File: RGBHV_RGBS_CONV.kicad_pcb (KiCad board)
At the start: 2 copper layers, 100 x 100 mm, 42 parts, among them J1 DIGITAL RGB, J10 ENABLE_SYNC_DIVIDE, J11 RGBHV_2, J12 LOGIC_SINGLE, J13 LOGIC_DOUBLE, J14 ENABLE_SYNC_MARGE, J15 RGBS_2, J16 RGBS_1, J17 +5V IN, J18 +5V OUT, J2 VGA DB15, J3 ANALOG RGB DB15, J4 X1, J5 DIGITAL_RGBHV_1, J6 ANALOG RGB, J7 DIGITAL_RGBHV_2, J8 ANALOG RGB VGA, J9 RGBHV_1, U1 LM1881, U2 74HC86

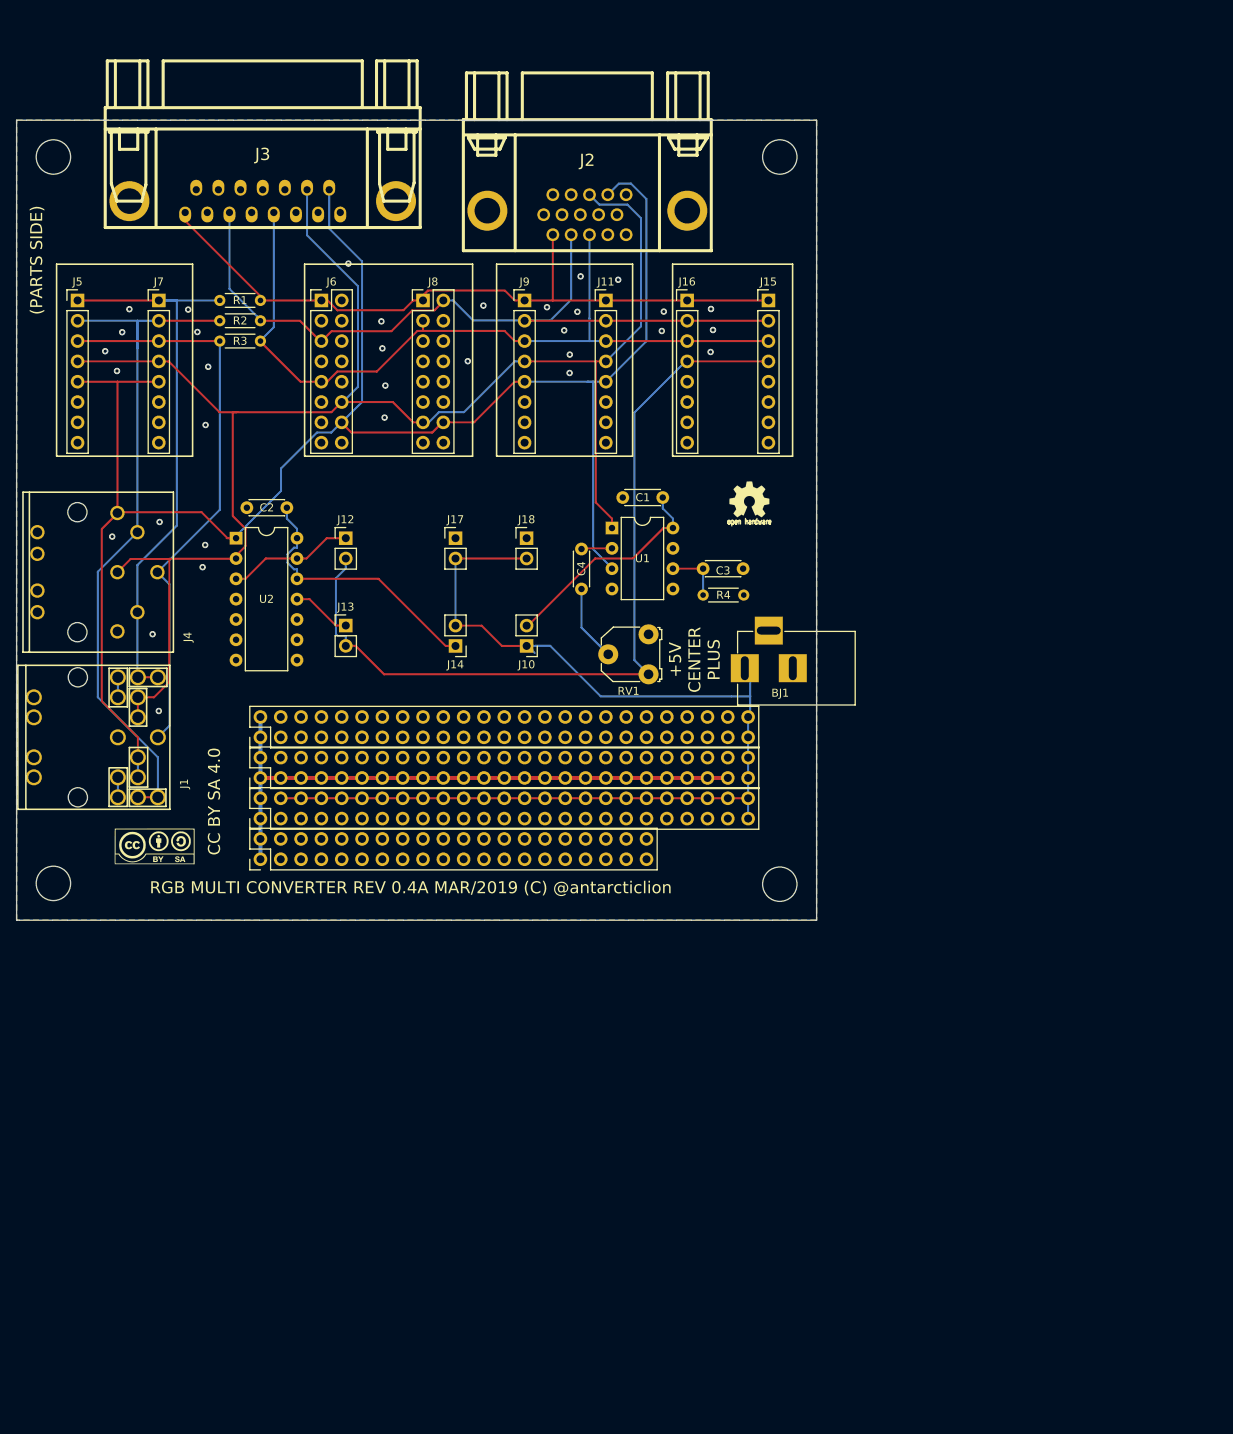
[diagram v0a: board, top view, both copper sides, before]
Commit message: Rev.5A DIn8 fix and remove sync sep.
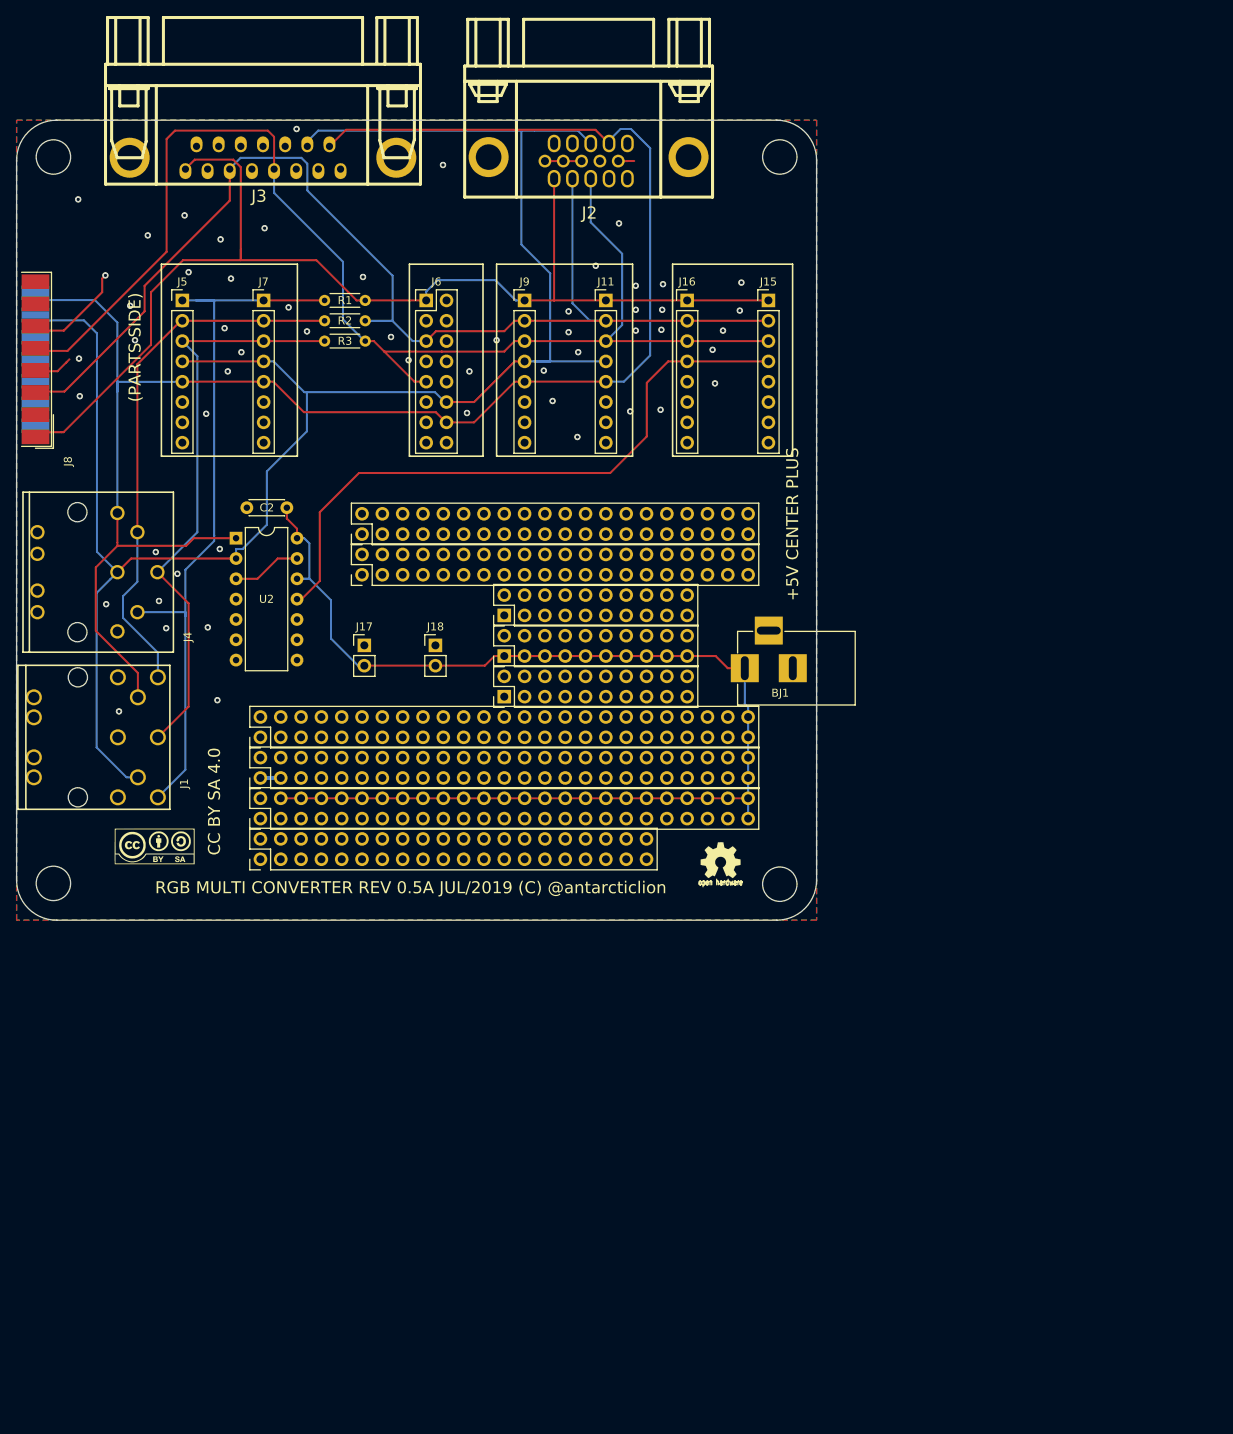
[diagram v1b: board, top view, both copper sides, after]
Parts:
- removed C1, C3, C4: 0.1uF, Capacitors_ThroughHole:C_Disc_D4.3mm_W1.9mm_P5.00mm
- removed J10: ENABLE_SYNC_DIVIDE, Pin_Headers:Pin_Header_Straight_1x02_Pitch2.54mm
- removed J12: LOGIC_SINGLE, Pin_Headers:Pin_Header_Straight_1x02_Pitch2.54mm
- removed J13: LOGIC_DOUBLE, Pin_Headers:Pin_Header_Straight_1x02_Pitch2.54mm
- removed J14: ENABLE_SYNC_MARGE, Pin_Headers:Pin_Header_Straight_1x02_Pitch2.54mm
- removed R4: 680KR, Resistors_ThroughHole:R_Axial_DIN0204_L3.6mm_D1.6mm_P5.08mm_Horizontal
- removed RV1: 1KR, Potentiometers:Potentiometer_Triwood_RM-065
- removed U1: LM1881, Housings_DIP:DIP-8_W7.62mm
- added JA5: PinHeader_2x10_P2.54mm_Vertical, Connector_PinHeader_2.54mm:PinHeader_2x10_P2.54mm_Vertical, F.Cu at (61.0, 72.1)
- added JA6: PinHeader_2x10_P2.54mm_Vertical, Connector_PinHeader_2.54mm:PinHeader_2x10_P2.54mm_Vertical, F.Cu at (61.0, 67.0)
- added JA7: PinHeader_2x10_P2.54mm_Vertical, Connector_PinHeader_2.54mm:PinHeader_2x10_P2.54mm_Vertical, F.Cu at (61.0, 61.9)
- added JA8: Pin_Header_Straight_2x20_Pitch2.54mm, Pin_Headers:Pin_Header_Straight_2x20_Pitch2.54mm, F.Cu at (43.2, 56.8)
- added JA9: Pin_Header_Straight_2x20_Pitch2.54mm, Pin_Headers:Pin_Header_Straight_2x20_Pitch2.54mm, F.Cu at (43.2, 51.7)
- C2: value 0.1uF -> C
- J15: value RGBS_2 -> RGBS_OUT
- J16: value RGBS_1 -> RGBS_OUT
- J3: value ANALOG RGB DB15 -> ANALOG RGB DA15
- J8: value ANALOG RGB VGA -> ANALOG RGB DA15 EDGE; footprint Pin_Headers:Pin_Header_Straight_2x08_Pitch2.54mm -> Connector_Dsub:DSUB-15_Female_EdgeMount_P2.77mm
- moved J8 49.0 mm to (2.36, 29.9), turned to 270 degrees
- moved G3 45.2 mm to (88.0, 92.5)
- moved G4 45.0 mm to (89.0, 92.5)
- moved J17 17.6 mm to (43.5, 65.6)
- moved J18 17.6 mm to (52.4, 65.6)
- moved J6 13.1 mm to (51.2, 22.5)
- moved R1 13.1 mm to (38.5, 22.5)
- moved R2 13.1 mm to (38.5, 25.1)
- moved R3 13.1 mm to (38.5, 27.6)
- moved J5 13.1 mm to (20.7, 22.5)
- moved J7 13.1 mm to (30.9, 22.5)
- moved J2 6.70 mm to (71.5, -5.50)
- moved J3 5.42 mm to (30.8, -2.42)
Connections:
- C2 pad 1: Net-(C2-Pad1) -> +5V
- J2 pad : GND -> (no net)
- J3 pad : GND -> (no net)
- J8 pad 10: GND -> Net-(J8-Pad10)
- J8 pad 11: GND -> Net-(J8-Pad11)
- J8 pad 13: HSYNC -> Net-(J8-Pad13)
- J8 pad 14: VSYNC -> HSYNC
- J8 pad 15: Net-(J8-Pad15) -> VSYNC
- J8 pad 2: G -> GND
- J8 pad 3: B -> G
- J8 pad 4: Net-(J8-Pad4) -> GND
- J8 pad 5: Net-(J8-Pad5) -> B
- J8 pad 7: GND -> Net-(J8-Pad7)
- J8 pad 8: GND -> Net-(J8-Pad8)
- U2 pad 11: Net-(J13-Pad1) -> CSYNC
- U2 pad 12: Net-(C2-Pad1) -> +5V
- U2 pad 14: Net-(C2-Pad1) -> +5V
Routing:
- net B: track 100.1 -> 160.5 mm
- net R: track 89.5 -> 144.7 mm
- net G: track 98.0 -> 150.7 mm
- net GND: track 76.4 -> 25.3 mm, vias 33 -> 56
- net Net-(C2-Pad1): track 34.1 -> 0.00 mm
- net Net-(C1-Pad1): track 27.7 -> 0.00 mm
- net HSYNC: track 210.7 -> 235.5 mm
- net CSYNC: track 104.7 -> 80.2 mm
- net DIGITAL_G: track 88.5 -> 67.3 mm
- net DIGITAL_R: track 72.4 -> 91.5 mm
- net +5V: track 136.3 -> 153.9 mm
- net Net-(C4-Pad1): track 9.55 -> 0.00 mm
- net Net-(J13-Pad1): track 7.46 -> 0.00 mm
- net Net-(U2-Pad13): track 15.8 -> 8.67 mm
- net Net-(C3-Pad1): track 7.07 -> 0.00 mm
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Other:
- outline, holes or cut-outs redrawn
- board text added: "RGB MULTI CONVERTER REV 0.5A JUL/2019 (C) @antarcticlion"
- board text removed: "RGB MULTI CONVERTER REV 0.4A MAR/2019 (C) @antarcticlion"

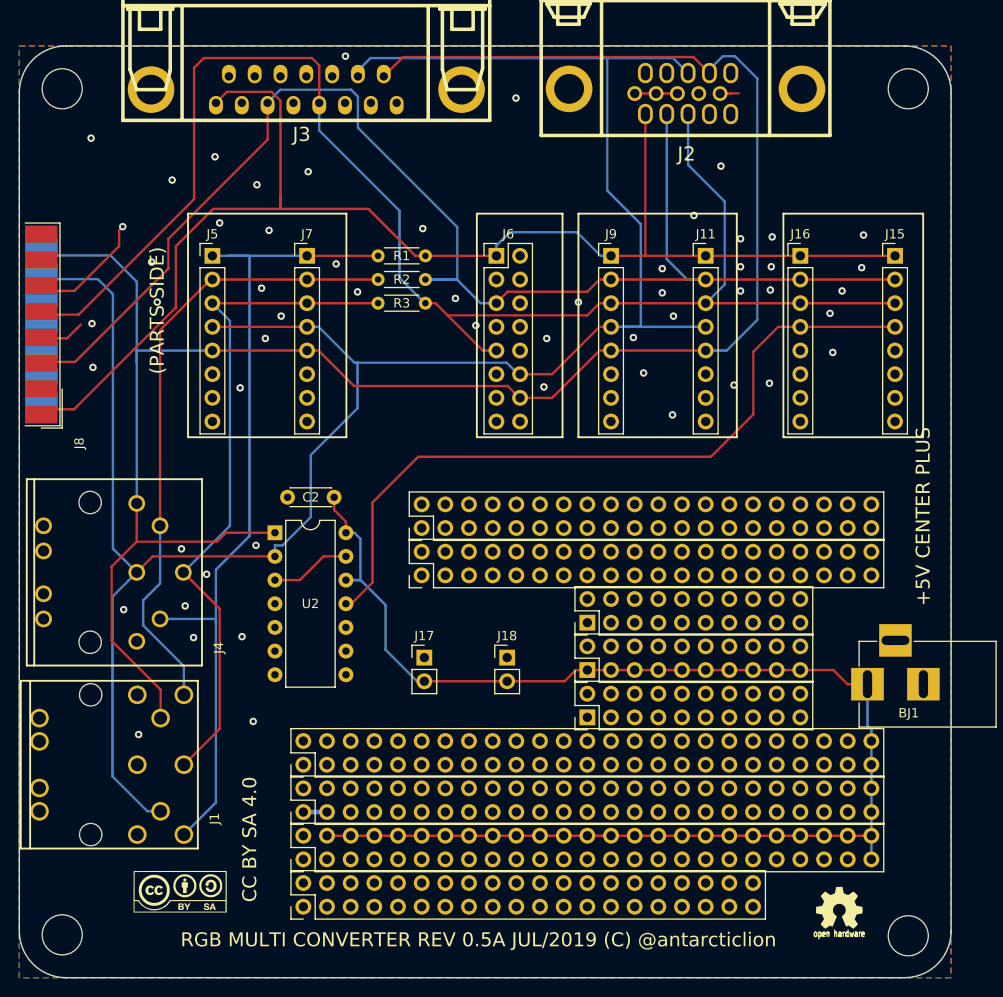
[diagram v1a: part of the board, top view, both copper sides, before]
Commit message: Rev.5B Add RGBS VR
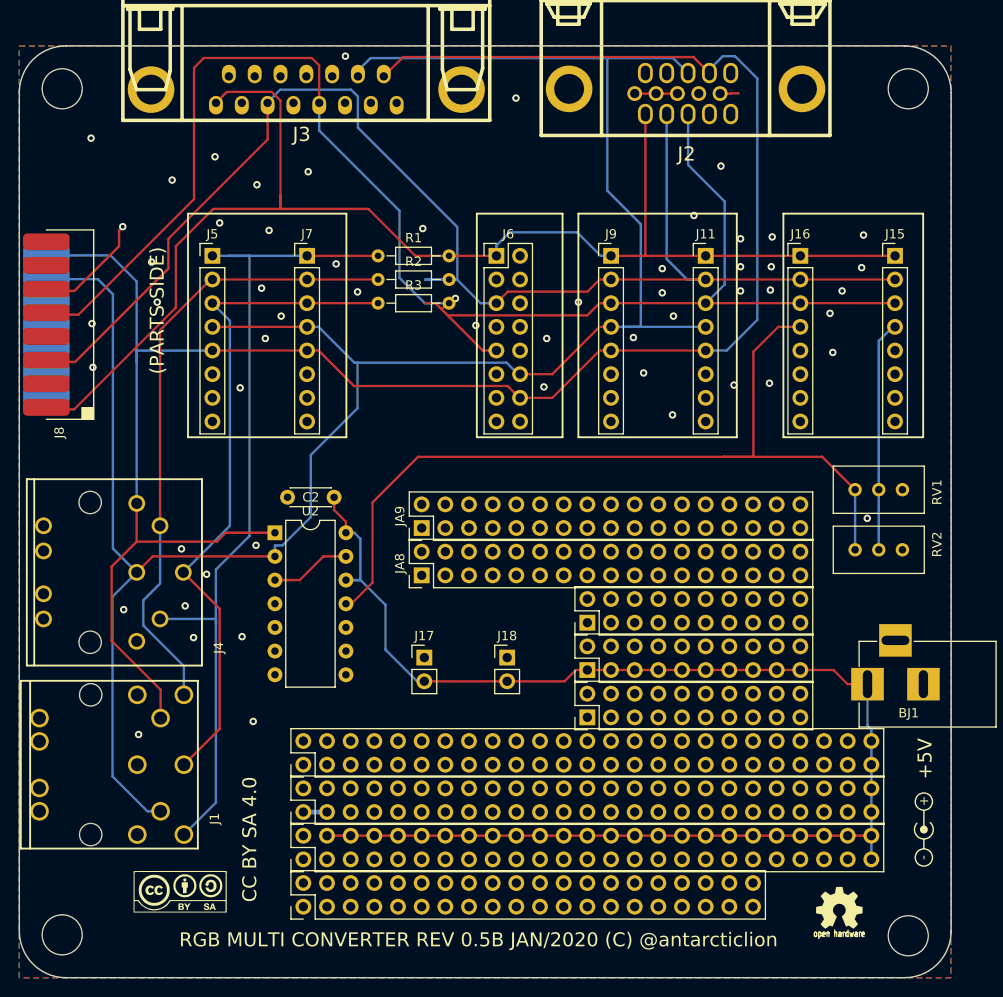
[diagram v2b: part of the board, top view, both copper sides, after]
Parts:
- added RV1: R_POT, Potentiometer_THT:Potentiometer_Bourns_3296W_Vertical, F.Cu at (94.8, 47.6)
- added RV2: R_POT, Potentiometer_THT:Potentiometer_Bourns_3296W_Vertical, F.Cu at (94.8, 54.1)
- added SYM1: Symbol_Barrel_Polarity, Symbol:Symbol_Barrel_Polarity, F.Cu at (97.0, 84.1)
- J11: value RGBHV_2 -> RGBHV_1
- J8: footprint Connector_Dsub:DSUB-15_Female_EdgeMount_P2.77mm -> ryuk_lib:D-SUB15_PCB_EDGE
- JA8, JA9: value Pin_Header_Straight_2x20_Pitch2.54mm -> PinHeader_2x17_P2.54mm_Vertical; footprint Pin_Headers:Pin_Header_Straight_2x20_Pitch2.54mm -> Connector_PinHeader_2.54mm:PinHeader_2x17_P2.54mm_Vertical
- R1, R2, R3: footprint Resistors_ThroughHole:R_Axial_DIN0204_L3.6mm_D1.6mm_P5.08mm_Horizontal -> Resistor_THT:R_Axial_DIN0204_L3.6mm_D1.6mm_P7.62mm_Horizontal
- U2: value 74HC86 -> 4070/74HC86; footprint Housings_DIP:DIP-14_W7.62mm -> Package_DIP:DIP-14_W7.62mm
- moved J8 8.93 mm to (2.90, 38.8), turned to 90 degrees
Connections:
- J15 pad 4: CSYNC -> CSYNC_RE
- JA8 pad 1: GND -> (no net)
- JA8 pad 2: GND -> (no net)
- JA9 pad 1: GND -> (no net)
- JA9 pad 2: GND -> (no net)
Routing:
- net CSYNC_RE: track 0.00 -> 24.8 mm
- net CSYNC: track 80.2 -> 94.7 mm
- net B: track 160.5 -> 165.3 mm, vias 0 -> 1
- net GND: track 25.3 -> 21.1 mm
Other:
- board text added: "+"
- board text added: "+5V"
- board text added: "-"
- board text added: "RGB MULTI CONVERTER REV 0.5B JAN/2020 (C) @antarcticlion"
- board text removed: "+5V CENTER PLUS"
- board text removed: "RGB MULTI CONVERTER REV 0.5A JUL/2019 (C) @antarcticlion"

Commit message: Rev1.0B
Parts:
- removed BJ1: BARREL_JACK, Connect:BARREL_JACK
- removed C2: C, Capacitors_ThroughHole:C_Disc_D4.3mm_W1.9mm_P5.00mm
- removed G1, G2: LOGO, w_logo:Logo_silk_CC-BY-SA_10x4.5mm
- removed G3, G4: LOGO, w_logo:Logo_silk_OSHW_6x6mm
- removed J18: +5V OUT, Pin_Headers:Pin_Header_Straight_1x02_Pitch2.54mm
- removed JA1: Pin_Header_Straight_2x20_Pitch2.54mm, Pin_Headers:Pin_Header_Straight_2x20_Pitch2.54mm
- removed JA2, JA3, JA4: Pin_Header_Straight_2x25_Pitch2.54mm, Pin_Headers:Pin_Header_Straight_2x25_Pitch2.54mm
- removed JA5, JA6, JA7: PinHeader_2x10_P2.54mm_Vertical, Connector_PinHeader_2.54mm:PinHeader_2x10_P2.54mm_Vertical
- removed JA8, JA9: PinHeader_2x17_P2.54mm_Vertical, Connector_PinHeader_2.54mm:PinHeader_2x17_P2.54mm_Vertical
- removed REF1, REF2, REF3, REF4: MountingHole_4.3mm_M4, Mounting_Holes:MountingHole_4.3mm_M4
- removed RV1, RV2: R_POT, Potentiometer_THT:Potentiometer_Bourns_3296W_Vertical
- removed SYM1: Symbol_Barrel_Polarity, Symbol:Symbol_Barrel_Polarity
- added C1: 0.1uF, Capacitor_THT:C_Disc_D5.0mm_W2.5mm_P5.00mm, F.Cu at (109.5, 98.9)
- added C3: 10uF, Capacitor_THT:C_Disc_D5.0mm_W2.5mm_P5.00mm, F.Cu at (136.3, 78.0)
- added C4: 0.1uF, Capacitor_THT:C_Disc_D5.0mm_W2.5mm_P5.00mm, F.Cu at (136.3, 82.8)
- added C5: 10uF, Capacitor_THT:C_Disc_D5.0mm_W2.5mm_P5.00mm, F.Cu at (141.0, 105.3)
- added C6: 0.1uF, Capacitor_THT:C_Disc_D5.0mm_W2.5mm_P5.00mm, F.Cu at (140.9, 100.4)
- added H1: M4, MountingHole:MountingHole_4.3mm_M4_Pad, F.Cu at (145.0, 157.0)
- added H2: M4, MountingHole:MountingHole_4.3mm_M4_Pad, F.Cu at (55.0, 67.0)
- added H3: M4, MountingHole:MountingHole_4.3mm_M4_Pad, F.Cu at (55.0, 157.0)
- added H4: M4, MountingHole:MountingHole_4.3mm_M4_Pad, F.Cu at (145.0, 67.0)
- added J10: AUDIO1, ryuk_lib:PJ-3900-04, F.Cu at (100.4, 63.5)
- added J12: AUDIO2, ryuk_lib:PJ-3900-04, F.Cu at (100.4, 93.4)
- added PIN**: Pin_2.54, ryuk_lib:Pin_2.54, F.Cu at (144.0, 126.4)
- added PIN**: Pin_2.54, ryuk_lib:Pin_2.54, F.Cu at (131.3, 126.4)
- added PIN**: Pin_2.54, ryuk_lib:Pin_2.54, F.Cu at (138.9, 129.0)
- added PIN**: Pin_2.54, ryuk_lib:Pin_2.54, F.Cu at (136.4, 129.0)
- added PIN**: Pin_2.54, ryuk_lib:Pin_2.54, F.Cu at (136.4, 121.4)
- added PIN**: Pin_2.54, ryuk_lib:Pin_2.54, F.Cu at (133.8, 121.4)
- added PIN**: Pin_2.54, ryuk_lib:Pin_2.54, F.Cu at (131.3, 121.4)
- added PIN**: Pin_2.54, ryuk_lib:Pin_2.54, F.Cu at (136.4, 123.9)
- added PIN**: Pin_2.54, ryuk_lib:Pin_2.54, F.Cu at (138.9, 123.9)
- added PIN**: Pin_2.54, ryuk_lib:Pin_2.54, F.Cu at (144.0, 123.9)
- added PIN**: Pin_2.54, ryuk_lib:Pin_2.54, F.Cu at (131.3, 123.9)
- added PIN**: Pin_2.54, ryuk_lib:Pin_2.54, F.Cu at (144.0, 129.0)
- added PIN**: Pin_2.54, ryuk_lib:Pin_2.54, F.Cu at (133.8, 123.9)
- added PIN**: Pin_2.54, ryuk_lib:Pin_2.54, F.Cu at (138.9, 121.4)
- added PIN**: Pin_2.54, ryuk_lib:Pin_2.54, F.Cu at (141.4, 121.4)
- added PIN**: Pin_2.54, ryuk_lib:Pin_2.54, F.Cu at (141.4, 123.9)
- added PIN**: Pin_2.54, ryuk_lib:Pin_2.54, F.Cu at (144.0, 121.4)
- added PIN**: Pin_2.54, ryuk_lib:Pin_2.54, F.Cu at (131.3, 116.3)
- added PIN**: Pin_2.54, ryuk_lib:Pin_2.54, F.Cu at (131.3, 118.8)
- added PIN**: Pin_2.54, ryuk_lib:Pin_2.54, F.Cu at (133.8, 118.8)
- added PIN**: Pin_2.54, ryuk_lib:Pin_2.54, F.Cu at (133.8, 116.3)
- added PIN**: Pin_2.54, ryuk_lib:Pin_2.54, F.Cu at (136.4, 118.8)
- added PIN**: Pin_2.54, ryuk_lib:Pin_2.54, F.Cu at (136.4, 126.4)
- added PIN**: Pin_2.54, ryuk_lib:Pin_2.54, F.Cu at (138.9, 118.8)
- added PIN**: Pin_2.54, ryuk_lib:Pin_2.54, F.Cu at (141.4, 118.8)
- added PIN**: Pin_2.54, ryuk_lib:Pin_2.54, F.Cu at (144.0, 118.8)
- added PIN**: Pin_2.54, ryuk_lib:Pin_2.54, F.Cu at (136.4, 116.3)
- added PIN**: Pin_2.54, ryuk_lib:Pin_2.54, F.Cu at (138.9, 116.3)
- added PIN**: Pin_2.54, ryuk_lib:Pin_2.54, F.Cu at (141.4, 116.3)
- added PIN**: Pin_2.54, ryuk_lib:Pin_2.54, F.Cu at (144.0, 116.3)
- added PIN**: Pin_2.54, ryuk_lib:Pin_2.54, F.Cu at (131.3, 129.0)
- added PIN**: Pin_2.54, ryuk_lib:Pin_2.54, F.Cu at (141.4, 129.0)
- added PIN**: Pin_2.54, ryuk_lib:Pin_2.54, F.Cu at (133.8, 129.0)
- added PIN**: Pin_2.54, ryuk_lib:Pin_2.54, F.Cu at (141.4, 126.4)
- added PIN**: Pin_2.54, ryuk_lib:Pin_2.54, F.Cu at (133.8, 126.4)
- added PIN**: Pin_2.54, ryuk_lib:Pin_2.54, F.Cu at (138.9, 126.4)
- added R10: 0R-NO_LOAD, Resistor_THT:R_Axial_DIN0207_L6.3mm_D2.5mm_P10.16mm_Horizontal, F.Cu at (124.5, 104.0)
- added R11: 100R-NO_LOAD, Resistor_THT:R_Axial_DIN0207_L6.3mm_D2.5mm_P10.16mm_Horizontal, F.Cu at (114.5, 89.5)
- added R4: 0R-NO_LOAD, Resistor_THT:R_Axial_DIN0207_L6.3mm_D2.5mm_P10.16mm_Horizontal, F.Cu at (109.5, 130.0)
- added R5: 150R, Resistor_THT:R_Axial_DIN0207_L6.3mm_D2.5mm_P10.16mm_Horizontal, F.Cu at (114.5, 130.0)
- added R6: 150R, Resistor_THT:R_Axial_DIN0207_L6.3mm_D2.5mm_P10.16mm_Horizontal, F.Cu at (119.5, 130.0)
- added R7: 0R-NO_LOAD, Resistor_THT:R_Axial_DIN0207_L6.3mm_D2.5mm_P10.16mm_Horizontal, F.Cu at (124.5, 130.0)
- added R8: 10KR, Resistor_THT:R_Axial_DIN0207_L6.3mm_D2.5mm_P10.16mm_Horizontal, F.Cu at (114.5, 104.0)
- added R9: 150R, Resistor_THT:R_Axial_DIN0207_L6.3mm_D2.5mm_P10.16mm_Horizontal, F.Cu at (119.5, 104.0)
- added U1: OUT_GND_IN_3.3V, Package_TO_SOT_THT:TO-220-3_Vertical, F.Cu at (133.2, 89.0)
- added U3: OUT_IN_GND_3.3V, Package_TO_SOT_THT:TO-220-3_Vertical, F.Cu at (142.2, 89.0)
- J1: footprint ryuk_org_lib:DIN 8 PCB -> ryuk_lib:DIN 8 PCB
- J11: value RGBHV_1 -> RGBHV_2; footprint Pin_Headers:Pin_Header_Straight_1x08_Pitch2.54mm -> Connector_JST:JST_XH_B8B-XH-A_1x08_P2.50mm_Vertical
- J15: value RGBS_OUT -> RGBS_OUT1; footprint Pin_Headers:Pin_Header_Straight_1x08_Pitch2.54mm -> Connector_JST:JST_XH_B8B-XH-A_1x08_P2.50mm_Vertical
- J16: value RGBS_OUT -> RGBS_OUT2; footprint Pin_Headers:Pin_Header_Straight_1x08_Pitch2.54mm -> Connector_JST:JST_XH_S8B-XH-A_1x08_P2.50mm_Horizontal
- J17: value +5V IN -> VIN; footprint Pin_Headers:Pin_Header_Straight_1x02_Pitch2.54mm -> Connector_JST:JST_XH_S2B-XH-A_1x02_P2.50mm_Horizontal
- J2: footprint ryuk_org_lib:DB_15F-VGA_L -> ryuk_lib:DB_15F-VGA_L
- J3: footprint w_conn_d-sub:DB_15F -> Connector_Dsub:DSUB-15_Female_Horizontal_P2.77x2.84mm_EdgePinOffset4.94mm_Housed_MountingHolesOffset7.48mm
- J4: footprint ryuk_org_lib:DIN 6 PCB SDS-60J -> ryuk_lib:DIN_6_PCB
- J5, J7, J9: footprint Pin_Headers:Pin_Header_Straight_1x08_Pitch2.54mm -> Connector_JST:JST_XH_B8B-XH-A_1x08_P2.50mm_Vertical
- J6: footprint Pin_Headers:Pin_Header_Straight_2x08_Pitch2.54mm -> Connector_IDC:IDC-Header_2x08_P2.54mm_Vertical
- J8: value ANALOG RGB DA15 EDGE -> SWITCHER; footprint ryuk_lib:D-SUB15_PCB_EDGE -> Connector_IDC:IDC-Header_2x05_P2.54mm_Vertical
- R1, R2, R3: footprint Resistor_THT:R_Axial_DIN0204_L3.6mm_D1.6mm_P7.62mm_Horizontal -> Resistor_THT:R_Axial_DIN0207_L6.3mm_D2.5mm_P10.16mm_Horizontal
- U2: value 4070/74HC86 -> 74HC86
- moved J3 182.4 mm to (129.8, 150.8), turned to 0 degrees
- moved J6 140.1 mm to (129.8, 138.5), turned to 270 degrees
- moved J7 124.7 mm to (83.9, 135.4), turned to 180 degrees
- moved J5 120.7 mm to (83.9, 125.4), turned to 180 degrees
- moved J4 108.7 mm to (69.3, 152.1), turned to 0 degrees
- moved J1 108.6 mm to (88.8, 152.1), turned to 0 degrees
- moved R1 105.8 mm to (83.9, 118.1), turned to 90 degrees
- moved U2 103.8 mm to (109.5, 115.7), turned to 90 degrees
- moved R2 102.4 mm to (81.4, 118.1), turned to 90 degrees
- moved R3 99.1 mm to (78.9, 118.0), turned to 90 degrees
- moved J17 94.0 mm to (137.4, 69.0), turned to 180 degrees
- moved J8 81.0 mm to (70.4, 83.5)
- moved J11 80.5 mm to (83.9, 102.4), turned to 180 degrees
- moved J9 74.9 mm to (83.9, 94.6), turned to 180 degrees
- moved J15 67.2 mm to (128.9, 80.0), turned to 180 degrees
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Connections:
- J11 pad 6: Net-(J11-Pad6) -> AUDIO_L
- J11 pad 7: Net-(J11-Pad7) -> AUDIO_R
- J15 pad 4: CSYNC_RE -> CSYNC
- J15 pad 5: Net-(J15-Pad5) -> VSYNC
- J15 pad 6: Net-(J15-Pad6) -> AUDIO_L
- J15 pad 7: Net-(J15-Pad7) -> AUDIO_R
- J16 pad 5: Net-(J16-Pad5) -> VSYNC
- J16 pad 6: Net-(J16-Pad6) -> AUDIO_L
- J16 pad 7: Net-(J16-Pad7) -> AUDIO_R
- J17 pad 2: +5V -> Net-(C3-Pad1)
- J3 pad 10: Net-(J3-Pad10) -> AUDIO_L
- J3 pad 11: Net-(J3-Pad11) -> AUDIO_R
- J3 pad 12: Net-(J3-Pad12) -> GND
- J3 pad 8: Net-(J3-Pad8) -> GND
- J5 pad 6: Net-(J5-Pad6) -> AUDIO_L
- J5 pad 7: Net-(J5-Pad7) -> AUDIO_R
- J6 pad 15: Net-(J6-Pad15) -> GND
- J6 pad 4: Net-(J6-Pad4) -> AUDIO_L
- J6 pad 6: Net-(J6-Pad6) -> AUDIO_R
- J6 pad 8: Net-(J6-Pad8) -> GND
- J7 pad 6: Net-(J7-Pad6) -> AUDIO_L
- J7 pad 7: Net-(J7-Pad7) -> AUDIO_R
- J8 pad 10: Net-(J8-Pad10) -> GND
- J8 pad 2: GND -> G
- J8 pad 3: G -> B
- J8 pad 4: GND -> HSYNC
- J8 pad 5: B -> VSYNC
- J8 pad 7: Net-(J8-Pad7) -> AUDIO_L
- J8 pad 8: Net-(J8-Pad8) -> AUDIO_R
- J8 pad 9: Net-(J8-Pad9) -> GND
- J9 pad 6: Net-(J9-Pad6) -> AUDIO_L
- J9 pad 7: Net-(J9-Pad7) -> AUDIO_R
- U2 pad 1: VSYNC -> Net-(R4-Pad2)
- U2 pad 10: Net-(U2-Pad10) -> GND
- U2 pad 11: CSYNC -> Net-(R10-Pad1)
- U2 pad 12: +5V -> Net-(U2-Pad12)
- U2 pad 13: Net-(U2-Pad13) -> Net-(R8-Pad1)
- U2 pad 14: +5V -> +3V3
- U2 pad 2: HSYNC -> Net-(R6-Pad2)
- U2 pad 3: Net-(U2-Pad13) -> Net-(U2-Pad12)
- U2 pad 4: Net-(U2-Pad4) -> GND
- U2 pad 5: Net-(U2-Pad5) -> GND
- U2 pad 9: Net-(U2-Pad9) -> GND
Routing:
- net GND: track 21.1 -> 454.1 mm, vias 56 -> 8
- net AUDIO_L: track 0.00 -> 194.9 mm
- net AUDIO_R: track 0.00 -> 191.8 mm
- net +5V: track 153.9 -> 0.00 mm
- net +3V3: track 0.00 -> 76.1 mm
- net CSYNC: track 94.7 -> 33.1 mm
- net DIGITAL_R: track 91.5 -> 35.7 mm
- net R: track 144.9 -> 197.5 mm
- net G: track 150.9 -> 199.5 mm
- net HSYNC: track 235.8 -> 188.6 mm
- net Net-(C3-Pad1): track 0.00 -> 31.1 mm
- net DIGITAL_B: track 73.4 -> 45.3 mm
- net CSYNC_RE: track 24.8 -> 0.00 mm
- net Net-(R6-Pad2): track 0.00 -> 14.1 mm
- net Net-(R10-Pad1): track 0.00 -> 10.0 mm
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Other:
- board text added: "+5_12V"
- board text added: "GND"
- board text added: "RGB MULTI CONVERTER REV 1.0B MAY/2021 (C) @antarcticlion"
- board text removed: "+"
- board text removed: "+5V"
- board text removed: "-"
- board text removed: "ANALOG RGB HV"
- board text removed: "ANALOG RGB S"
- board text removed: "CC BY SA 4.0"
- board text removed: "DIGITAL RGB HV"
- board text removed: "RGB MULTI CONVERTER REV 0.5B JAN/2020 (C) @antarcticlion"
